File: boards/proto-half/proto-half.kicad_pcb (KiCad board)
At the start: 2 copper layers, 47 x 95 mm, 42 parts, among them J1 Conn_01x12, J10 Conn_01x12, J11 Conn_01x12, J12 Conn_01x12, J13 Conn_01x12, J14 Conn_01x12, J15 Conn_01x12, J16 Conn_01x12, J17 Conn_01x12, J18 Conn_01x12, J19 Conn_01x12, J2 Conn_01x12, J20 Conn_01x12, J21 Conn_01x12, J22 Conn_01x12, J23 Conn_01x12, J24 Conn_01x12, J25 Conn_01x12, J26 Conn_01x12, J27 Conn_01x12, J28 Conn_01x12, J29 Conn_01x12, J3 Conn_01x12, J30 Conn_01x12, J31 Conn_01x06, J32 Conn_01x06, J33 Conn_01x30, J34 Conn_01x30, J35 Conn_01x22, J36 Conn_01x22, J37 Conn_01x04_MountingPin, J38 Conn_01x04_MountingPin, J4 Conn_01x12, J5 Conn_01x12, J6 Conn_01x12, J7 Conn_01x12, J8 Conn_01x12, J9 Conn_01x12

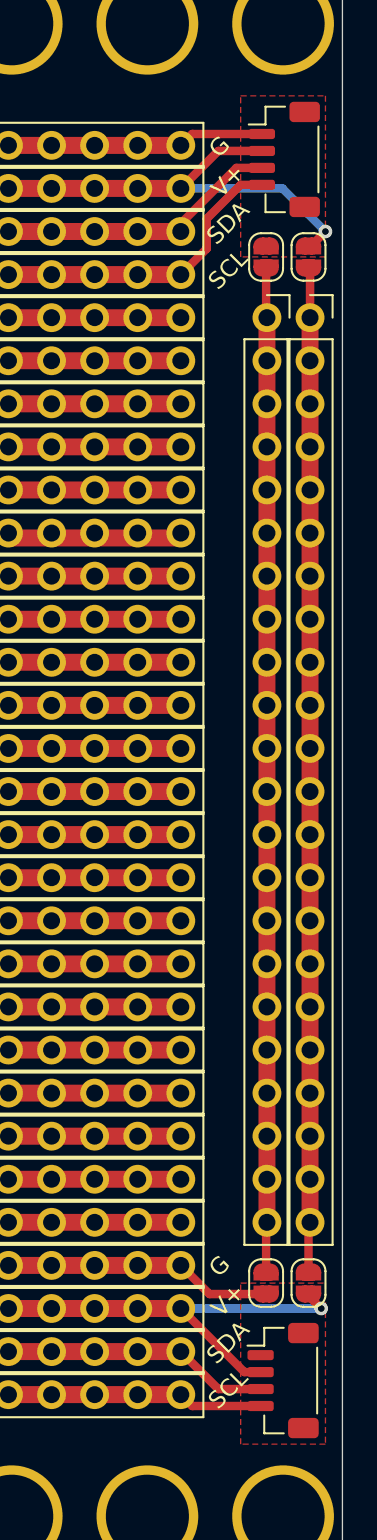
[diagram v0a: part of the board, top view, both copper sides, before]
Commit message: Start to fix the proto board connectors.
Half board is fixed, quarter board requires reducing the length of a couple
of the connectors, namely the power rails and the top-right proto line.
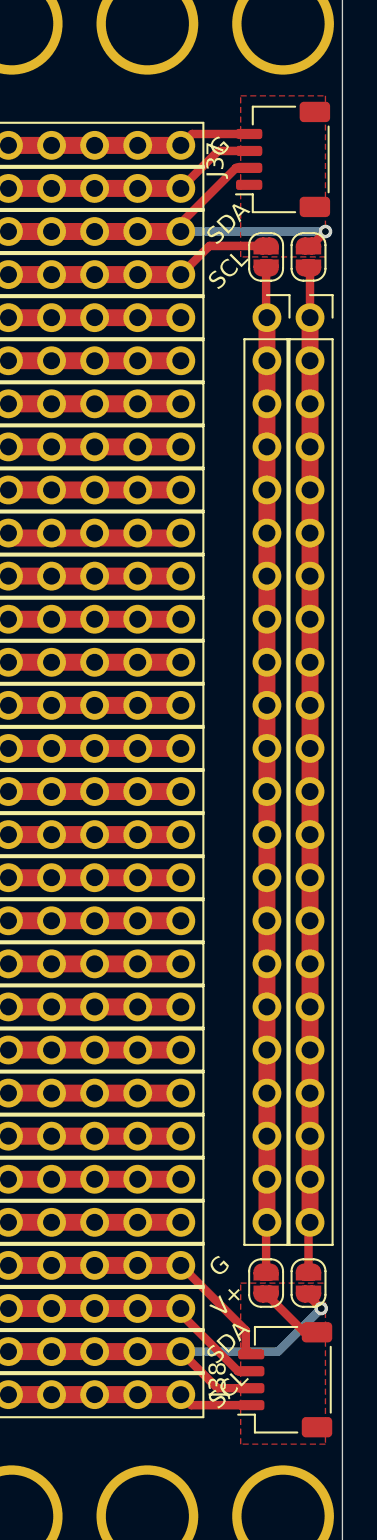
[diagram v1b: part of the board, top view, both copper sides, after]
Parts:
- J37, J38: footprint Connector_JST:JST_SH_BM04B-SRSS-TB_1x04-1MP_P1.00mm_Vertical -> Connector_JST:JST_SH_SM04B-SRSS-TB_1x04-1MP_P1.00mm_Horizontal
- moved J38 0.13 mm to (144.1, 124.0), turned to 90 degrees
- moved J37 0.07 mm to (144.0, 52.0), turned to 90 degrees
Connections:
- J1 pad 10: /Q1-GND -> /Q1-SCL
- J1 pad 11: /Q1-GND -> /Q1-SCL
- J1 pad 12: /Q1-GND -> /Q1-SCL
- J1 pad 8: /Q1-GND -> /Q1-SCL
- J1 pad 9: /Q1-GND -> /Q1-SCL
- J2 pad 10: /Q1-3v3 -> /Q1-SDA
- J2 pad 11: /Q1-3v3 -> /Q1-SDA
- J2 pad 12: /Q1-3v3 -> /Q1-SDA
- J2 pad 8: /Q1-3v3 -> /Q1-SDA
- J2 pad 9: /Q1-3v3 -> /Q1-SDA
- J27 pad 10: /Q2-GND -> /Q2-SCL
- J27 pad 11: /Q2-GND -> /Q2-SCL
- J27 pad 12: /Q2-GND -> /Q2-SCL
- J27 pad 8: /Q2-GND -> /Q2-SCL
- J27 pad 9: /Q2-GND -> /Q2-SCL
- J28 pad 10: /Q2-3v3 -> /Q2-SDA
- J28 pad 11: /Q2-3v3 -> /Q2-SDA
- J28 pad 12: /Q2-3v3 -> /Q2-SDA
- J28 pad 8: /Q2-3v3 -> /Q2-SDA
- J28 pad 9: /Q2-3v3 -> /Q2-SDA
- J29 pad 10: /Q2-SDA -> /Q2-3v3
- J29 pad 11: /Q2-SDA -> /Q2-3v3
- J29 pad 12: /Q2-SDA -> /Q2-3v3
- J29 pad 8: /Q2-SDA -> /Q2-3v3
- J29 pad 9: /Q2-SDA -> /Q2-3v3
- J3 pad 10: /Q1-SDA -> /Q1-3v3
- J3 pad 11: /Q1-SDA -> /Q1-3v3
- J3 pad 12: /Q1-SDA -> /Q1-3v3
- J3 pad 8: /Q1-SDA -> /Q1-3v3
- J3 pad 9: /Q1-SDA -> /Q1-3v3
- J30 pad 10: /Q2-SCL -> /Q2-GND
- J30 pad 11: /Q2-SCL -> /Q2-GND
- J30 pad 12: /Q2-SCL -> /Q2-GND
- J30 pad 8: /Q2-SCL -> /Q2-GND
- J30 pad 9: /Q2-SCL -> /Q2-GND
- J4 pad 10: /Q1-SCL -> /Q1-GND
- J4 pad 11: /Q1-SCL -> /Q1-GND
- J4 pad 12: /Q1-SCL -> /Q1-GND
- J4 pad 8: /Q1-SCL -> /Q1-GND
- J4 pad 9: /Q1-SCL -> /Q1-GND
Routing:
- net /Q1-SCL: track 18.2 -> 14.5 mm
- net /Q2-GND: track 15.9 -> 18.5 mm
- net /Q2-SCL: track 15.1 -> 17.1 mm
- net /Q1-SDA: track 16.8 -> 15.1 mm
- net /Q1-GND: track 15.2 -> 15.9 mm
